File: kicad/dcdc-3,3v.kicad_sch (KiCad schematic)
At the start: 12 parts, among them U3 XL7005A

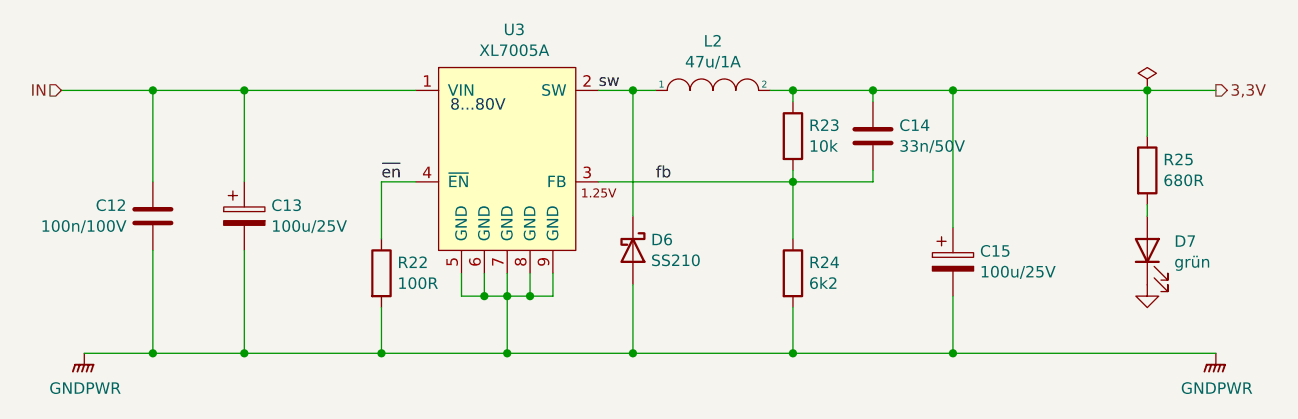
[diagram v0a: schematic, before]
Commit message: created bom for order lcsc
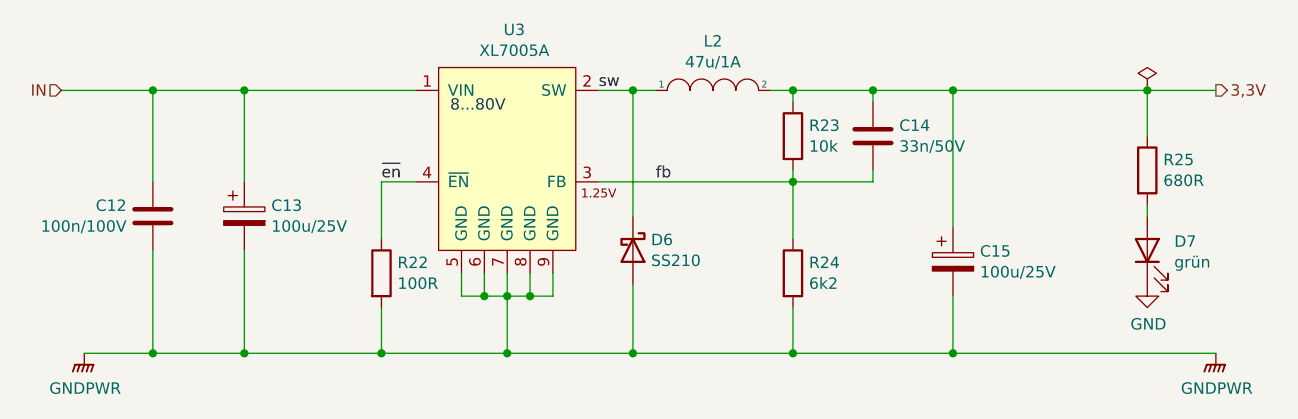
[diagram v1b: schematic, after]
